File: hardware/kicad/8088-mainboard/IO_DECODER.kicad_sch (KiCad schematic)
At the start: 2 parts, among them U12 74LS138

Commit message: Add PSB board design
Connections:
- net IO_EXP2_CS renamed IO_E0_FF
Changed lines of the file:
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@@
-		)
-	)
-	(wire
-		(pts
-			(xy 160.02 96.52) (xy 170.18 96.52)
-		)
-		(stroke
-			(width 0)
-			(type default)
 		)
 	)
@@
 		)
 	)
-	(label "IO_E0_FF"
-		(at 160.02 96.52 0)
-		(effects
-			(font
-				(size 1.27 1.27)
-			)
-			(justify left bottom)
-		)
-	)
 	(label "IO_C0_DF"
 		(at 147.32 93.98 180)
@@
 		)
 	)
-	(hierarchical_label "IO_EXP2_CS"
-		(shape input)
-		(at 170.18 96.52 0)
-		(effects
-			(font
-				(size 1.27 1.27)
-			)
-			(justify left)
-		)
-	)

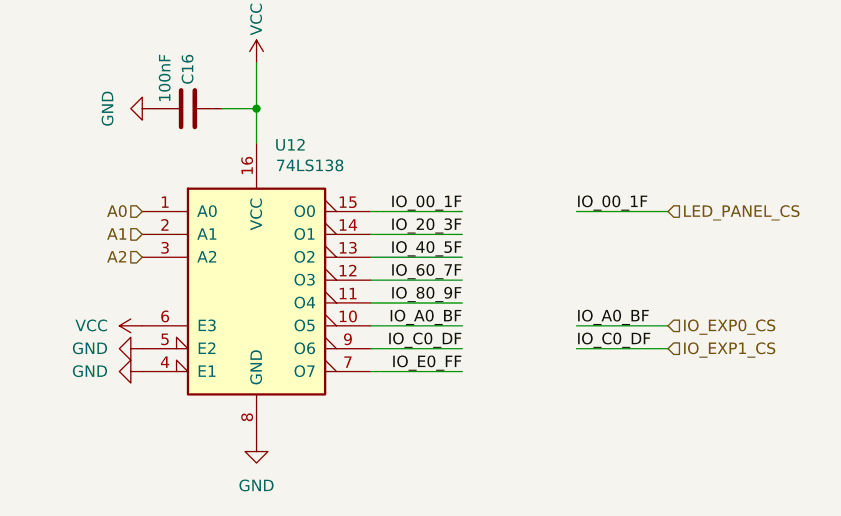
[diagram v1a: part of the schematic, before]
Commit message: Update 8088-mainboard schematics for refined connections and label adjustments
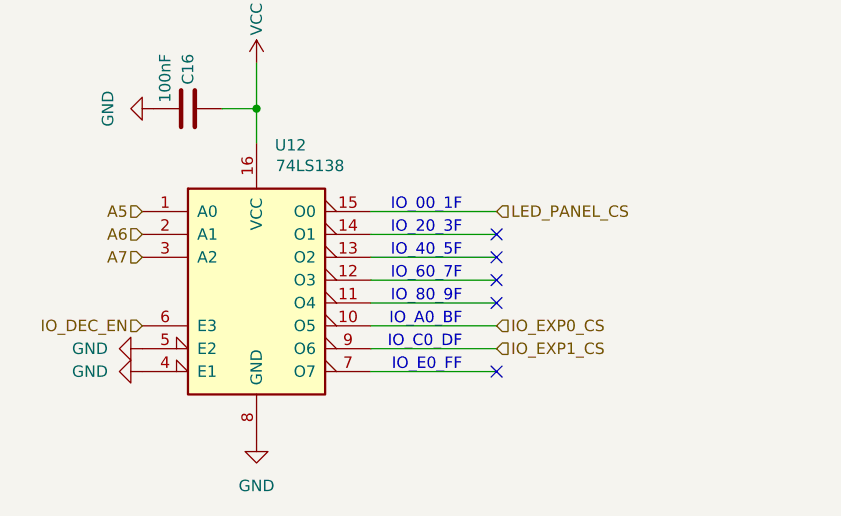
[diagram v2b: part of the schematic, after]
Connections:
- net VCC: no longer U12.6 (E3)
- net A0 renamed A5
- net A1 renamed A6
- net A2 renamed A7
- net IO_20_3F: no longer names the net of U12.14 (O1)
- net IO_40_5F: no longer names the net of U12.13 (O2)
- net IO_60_7F: no longer names the net of U12.12 (O3)
- net IO_80_9F: no longer names the net of U12.11 (O4)
- net IO_E0_FF: no longer names the net of U12.7 (O7)
- new net IO_DEC_EN: U12.6 (E3)
- no-connect marks 0 -> 5
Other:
- note added: "IO_00_1F"
- note added: "IO_20_3F"
- note added: "IO_40_5F"
- note added: "IO_60_7F"
- note added: "IO_80_9F"
- note added: "IO_A0_BF"
- note added: "IO_C0_DF"
- note added: "IO_E0_FF"

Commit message: Update 8086-mainboard scheme
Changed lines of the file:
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@@
+	(wire
+		(pts
+			(xy 139.7762 35.6362) (xy 142.3162 35.6362)
+		)
+		(stroke
+			(width 0)
+			(type default)
+		)
+	)
+	(wire
+		(pts
+			(xy 0.0762 0.0762) (xy 139.7762 0.0762)
+		)
+		(stroke
+			(width 0)
+			(type default)
+		)
+	)
 	(wire
 		(pts
@@
 		(pts
 			(xy 124.46 67.31) (xy 124.46 71.12)
+		)
+		(stroke
+			(width 0)
+			(type default)
+		)
+	)
+	(wire
+		(pts
+			(xy 139.7762 0.0762) (xy 139.7762 35.6362)
 		)
 		(stroke
@@
 	)
 	(hierarchical_label "IO_EXP1_CS"
-		(shape input)
+		(shape output)
 		(at 151.13 93.98 0)
 		(effects
@@
 	)
 	(hierarchical_label "IO_EXP0_CS"
-		(shape input)
+		(shape output)
 		(at 151.13 91.44 0)
 		(effects
@@
 	)
 	(hierarchical_label "LED_PANEL_CS"
-		(shape input)
+		(shape output)
 		(at 151.13 78.74 0)
 		(effects

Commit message: Update 8086-mainboard scheme
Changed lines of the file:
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@@
-	(wire
-		(pts
-			(xy 139.7762 35.6362) (xy 142.3162 35.6362)
-		)
-		(stroke
-			(width 0)
-			(type default)
-		)
-	)
-	(wire
-		(pts
-			(xy 0.0762 0.0762) (xy 139.7762 0.0762)
-		)
-		(stroke
-			(width 0)
-			(type default)
-		)
-	)
 	(wire
 		(pts
@@
 		)
 		(stroke
-			(width 0)
-			(type default)
-		)
-	)
-	(wire
-		(pts
-			(xy 139.7762 0.0762) (xy 139.7762 35.6362)
-		)
-		(stroke

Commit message: Update 8088-mainboard schematics
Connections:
- net IO_DEC_EN renamed IOM
- net LED_PANEL_CS: no longer names the net of U12.15 (O0)
- no-connect marks 5 -> 6
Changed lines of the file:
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@@
+	)
+	(no_connect
+		(at 151.13 78.74)
 	)
 	(no_connect
@@
 		)
 	)
-	(hierarchical_label "A5"
+	(hierarchical_label "IOM"
 		(shape input)
-		(at 111.76 78.74 180)
+		(at 111.76 91.44 180)
 		(effects
 			(font
@@
 		)
 	)
-	(hierarchical_label "IO_DEC_EN"
+	(hierarchical_label "A5"
 		(shape input)
-		(at 111.76 91.44 180)
+		(at 111.76 78.74 180)
 		(effects
 			(font
@@
 		(effects
 			(font
-				(size 1.27 1.27)
-			)
-			(justify left)
-		)
-	)
-	(hierarchical_label "LED_PANEL_CS"
-		(shape output)
-		(at 151.13 78.74 0)
-		(effects
-			(font

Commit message: Finalize 8088 mainboard rev1.0 for production
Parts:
- U7: renamed from U12; footprint Package_DIP:DIP-16_W7.62mm -> Package_DIP:DIP-16_W7.62mm_Socket
- renumbered C16 to C10
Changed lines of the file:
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@@
 		(dnp no)
 		(fields_autoplaced yes)
-		(property "Reference" "#PWR077"
+		(property "Reference" "#PWR040"
 			(at 106.68 67.31 0)
 			(hide yes)
@@
 			(project "8088-mainboard"
 				(path "/15ce4f45-6f32-456e-874c-aac11293789a/c64b3a1d-9cdf-4d26-8a62-60cbadd711b0"
-					(reference "#PWR077")
+					(reference "#PWR040")
 					(unit 1)
 				)
@@
 		(in_pos_files yes)
 		(dnp no)
-		(property "Reference" "U12"
+		(property "Reference" "U7"
 			(at 126.492 71.374 0)
 			(show_name no)
@@
 			)
 		)
-		(property "Footprint" "Package_DIP:DIP-16_W7.62mm"
+		(property "Footprint" "Package_DIP:DIP-16_W7.62mm_Socket"
 			(at 124.46 86.36 0)
 			(hide yes)
@@
 			(project "8088-mainboard"
 				(path "/15ce4f45-6f32-456e-874c-aac11293789a/c64b3a1d-9cdf-4d26-8a62-60cbadd711b0"
-					(reference "U12")
+					(reference "U7")
 					(unit 1)
 				)
@@
 		(in_pos_files yes)
 		(dnp no)
-		(property "Reference" "#PWR078"
+		(property "Reference" "#PWR041"
 			(at 124.46 66.04 0)
 			(hide yes)
@@
 			(project "8088-mainboard"
 				(path "/15ce4f45-6f32-456e-874c-aac11293789a/c64b3a1d-9cdf-4d26-8a62-60cbadd711b0"
-					(reference "#PWR078")
+					(reference "#PWR041")
 					(unit 1)
 				)
@@
 		(dnp no)
 		(fields_autoplaced yes)
-		(property "Reference" "#PWR079"
+		(property "Reference" "#PWR042"
 			(at 124.46 110.49 0)
 			(hide yes)
@@
 			(project "8088-mainboard"
 				(path "/15ce4f45-6f32-456e-874c-aac11293789a/c64b3a1d-9cdf-4d26-8a62-60cbadd711b0"
-					(reference "#PWR079")
+					(reference "#PWR042")
 					(unit 1)
 				)
@@
 		(dnp no)
 		(fields_autoplaced yes)
-		(property "Reference" "#PWR076"
+		(property "Reference" "#PWR039"
 			(at 105.41 96.52 0)
 			(hide yes)
@@
 			(project "8088-mainboard"
 				(path "/15ce4f45-6f32-456e-874c-aac11293789a/c64b3a1d-9cdf-4d26-8a62-60cbadd711b0"
-					(reference "#PWR076")
+					(reference "#PWR039")
 					(unit 1)
 				)
@@
 		(in_pos_files yes)
 		(dnp no)
-		(property "Reference" "C16"
+		(property "Reference" "C10"
 			(at 116.84 61.214 0)
 			(show_name no)
@@
 			(project "8088-mainboard"
 				(path "/15ce4f45-6f32-456e-874c-aac11293789a/c64b3a1d-9cdf-4d26-8a62-60cbadd711b0"
-					(reference "C16")
+					(reference "C10")
 					(unit 1)
 				)
@@
 		(dnp no)
 		(fields_autoplaced yes)
-		(property "Reference" "#PWR075"
+		(property "Reference" "#PWR038"
 			(at 105.41 93.98 0)
 			(hide yes)
@@
 			(project "8088-mainboard"
 				(path "/15ce4f45-6f32-456e-874c-aac11293789a/c64b3a1d-9cdf-4d26-8a62-60cbadd711b0"
-					(reference "#PWR075")
-					(unit 1)
-				)
+					(reference "#PWR038")
+					(unit 1)
+				)
